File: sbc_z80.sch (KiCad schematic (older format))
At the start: 61 parts, among them J1 RC80 Bus, J3 PIO Header, J4 Conn_01x06, J5 Conn_01x06, J6 CTC Header, J7 AVR-JTAG-10, SW1 SW_Push, SW2 Config, U1 CPU -Z84C0020AEG, U10 74HC04, U12 MIC811LUY, U3 SRAM - IS62C5128BL-45TLI, U4 SST39SF040, U6 SIO/3 - Z84C4310AEG, U7 CPLD - EPM7032STC44, U8 CTC - Z84C3010AEG, U9 Z84C2010AEG

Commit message: fixed pins
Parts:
- removed J7: AVR-JTAG-10, Connector_PinHeader_1.27mm:PinHeader_2x05_P1.27mm_Vertical, symbol sbc_z80-rescue:AVR-JTAG-10-Connector
- removed R21: 1K, Resistor_SMD:R_0603_1608Metric_Pad1.05x0.95mm_HandSolder, symbol sbc_z80-rescue:R_Small-Device
- removed R22, R23, R24: 10K, Resistor_SMD:R_0603_1608Metric_Pad1.05x0.95mm_HandSolder, symbol sbc_z80-rescue:R_Small-Device
- added J?: AVR-JTAG-10, Connector_PinHeader_1.27mm:PinHeader_2x05_P1.27mm_Vertical, symbol sbc_z80-rescue:AVR-JTAG-10-Connector
- added R?: 1K, Resistor_SMD:R_0603_1608Metric_Pad1.05x0.95mm_HandSolder, symbol sbc_z80-rescue:R_Small-Device
- added R? (x3): 10K, Resistor_SMD:R_0603_1608Metric_Pad1.05x0.95mm_HandSolder, symbol sbc_z80-rescue:R_Small-Device
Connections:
- wire segments 513 -> 490
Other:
- moved on the sheet: R31, R32, R33, R34, R35, R36, R5, R6, R7, R8, SW2, U1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

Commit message: changed part layout, removed switch
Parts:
- removed C10: 100nF, Capacitor_SMD:C_0603_1608Metric_Pad1.05x0.95mm_HandSolder, symbol sbc_z80-rescue:C_Small-Device
- removed J5: Conn_01x06, Connector_PinHeader_2.54mm:PinHeader_1x06_P2.54mm_Horizontal, symbol sbc_z80-rescue:Conn_01x06-Connector_Generic
- removed J?: AVR-JTAG-10, Connector_PinHeader_1.27mm:PinHeader_2x05_P1.27mm_Vertical, symbol sbc_z80-rescue:AVR-JTAG-10-Connector
- removed R10, R11, R12, R13, R17, R19: 2K2, Resistor_SMD:R_0603_1608Metric_Pad1.05x0.95mm_HandSolder, symbol sbc_z80-rescue:R_Small-Device
- removed R15, R20: 100K, Resistor_SMD:R_0603_1608Metric_Pad1.05x0.95mm_HandSolder, symbol sbc_z80-rescue:R_Small-Device
- removed R?: 1K, Resistor_SMD:R_0603_1608Metric_Pad1.05x0.95mm_HandSolder, symbol sbc_z80-rescue:R_Small-Device
- removed R? (x3): 10K, Resistor_SMD:R_0603_1608Metric_Pad1.05x0.95mm_HandSolder, symbol sbc_z80-rescue:R_Small-Device
- removed SW1: SW_Push, Button_Switch_SMD:SW_SPST_FSMSM, symbol sbc_z80-rescue:SW_Push-Switch
- removed SW2: Config, Button_Switch_SMD:SW_DIP_SPSTx06_Slide_Copal_CHS-06A_W5.08mm_P1.27mm_JPin, symbol sbc_z80-rescue:SW_DIP_x06-Switch
- removed U12: MIC811LUY, Package_TO_SOT_SMD:SOT-143, symbol sbc_z80-rescue:MIC811LUY-Power_Supervisor
- added C6: 100nF, Capacitor_SMD:C_0603_1608Metric_Pad1.05x0.95mm_HandSolder, symbol sbc_z80-rescue:C_Small-Device
- added C7: 2.2uF, Capacitor_SMD:C_0603_1608Metric_Pad1.05x0.95mm_HandSolder, symbol max_breakout-rescue:C_Small-Device
- added D1, D10, D11, D4, D5, D6, D7, D8, D9: Green, LED_SMD:LED_0603_1608Metric_Pad1.05x0.95mm_HandSolder, symbol max_breakout-rescue:LED-Device
- added D2: LED, LED_SMD:LED_0603_1608Metric_Pad1.05x0.95mm_HandSolder, symbol Device:LED
- added J3: AVR-JTAG-10, Connector_PinHeader_2.54mm:PinHeader_2x05_P2.54mm_Vertical, symbol max_breakout-rescue:AVR-JTAG-10-Connector
- added J4: IDE, Connector_PinHeader_2.54mm:PinHeader_2x20_P2.54mm_Horizontal, symbol Connector_Generic:Conn_02x20_Odd_Even
- added J7: Conn_01x06, Connector_PinHeader_2.54mm:PinHeader_1x06_P2.54mm_Horizontal, symbol sbc_z80-rescue:Conn_01x06-Connector_Generic
- added JP1: Jumper_NC_Small, Connector_PinHeader_1.27mm:PinHeader_1x02_P1.27mm_Vertical, symbol Device:Jumper_NC_Small
- added Q1: IRLML6402, Package_TO_SOT_SMD:SOT-23, symbol max_breakout-rescue:IRLML6402-Transistor_FET
- added R10: 1K, Resistor_SMD:R_0603_1608Metric_Pad1.05x0.95mm_HandSolder, symbol max_breakout-rescue:R_Small-Device
- added R12, R14, R15: 10K, Resistor_SMD:R_0603_1608Metric_Pad1.05x0.95mm_HandSolder, symbol max_breakout-rescue:R_Small-Device
- added R13, R3: 100R, Resistor_SMD:R_0603_1608Metric_Pad1.05x0.95mm_HandSolder, symbol max_breakout-rescue:R_Small-Device
- added R17: 360R, Resistor_SMD:R_0603_1608Metric_Pad1.05x0.95mm_HandSolder, symbol max_breakout-rescue:R_Small-Device
- added R21, R22, R6, R8, R9: 10K, Resistor_SMD:R_0603_1608Metric_Pad1.05x0.95mm_HandSolder, symbol sbc_z80-rescue:R_Small-Device
- added R23, R24, R25, R29, R30: 680R, Resistor_SMD:R_0603_1608Metric_Pad1.05x0.95mm_HandSolder, symbol sbc_z80-rescue:R_Small-Device
- added R37, R38: 2K2, Resistor_SMD:R_0603_1608Metric_Pad1.05x0.95mm_HandSolder, symbol sbc_z80-rescue:R_Small-Device
- added R40, R42: 100K, Resistor_SMD:R_0603_1608Metric_Pad1.05x0.95mm_HandSolder, symbol sbc_z80-rescue:R_Small-Device
- added SW1: Reset, Button_Switch_SMD:SW_Push_SPST_NO_Alps_SKRK, symbol Switch:SW_Push
- added U1: DS1813R-5+T&R, Package_TO_SOT_SMD:SOT-23, symbol max_breakout-rescue:DS1813R-5+T&R-Power_Supervisor
- added U11: 74HCT273, Package_SO:TSSOP-20_4.4x6.5mm_P0.65mm, symbol 74xx:74HCT273
- added U2: AP7381-33SA, Package_TO_SOT_SMD:SOT-23, symbol Regulator_Linear:AP7381-33SA
- added X1: CTX-636 50mhz, Oscillator:Oscillator_SMD_TXC_7C-4Pin_5.0x3.2mm_HandSoldering, symbol Oscillator:TXC-7C
- R16: value 2K2 -> 1K
- R18: value 2K2 -> 10K
- R26, R27, R28: value 10K -> 680R; Description (none) -> Thick Film Resistors - SMD 1K OHM 5%; MFR (none) -> Yageo; MPN (none) -> RC0603JR-071KL; SPN (none) -> 603-RC0603JR-071KL; SPR (none) -> Mouser; SPURL (none) -> https://www.mouser.com/ProductDetail/603-RC0603JR-071KL
- R31, R32, R33, R34, R35, R36: value 10K -> 2K2
- U10: renamed from U9; symbol sbc_z80-rescue:Z84C2010AEG-sbc_z80-rescue -> sbc_z80-rescue:Z84C2010AEG
- U7: renamed from U10; value 74HC04 -> 74HCT2G04; footprint (none) -> Package_SO:TSOP-6_1.65x3.05mm_P0.95mm; symbol sbc_z80-rescue:74HC04-74xx -> 74xGxx:74HCT2G04
- U8: renamed from U4; footprint (none) -> Package_LCC:PLCC-32_SMD-Socket
- renumbered C5 to C1, C13 to C10, C14 to C11, C6 to C2, C7 to C3, C8 to C4, C9 to C5, C11 to C8, C12 to C9, D1 to D3, J6 to J2, J3 to J5, J4 to J6, R5 to R1, R4 to R11, R29 to R19, R8 to R2, R30 to R20, R9 to R39, R7 to R4, R14 to R41, R6 to R5, R25 to R7, U1 to U3, U8 to U4, U7 to U5, U3 to U6, U6 to U9
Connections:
- net labels added: 3V3, CLK_50, CLK_CPU, DO, D_LED, ~ACTIVE, ~CF, ~PIO_RST
- net labels removed: +5V, CLK_F, SW0, SW1, SW2, SW3, SW4, SW5, SW6, ~DIO
- wire segments 490 -> 568
- no-connect marks 18 -> 25
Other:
- note added: "50Mhz Clock"
- note added: "IDE/CF"
- note added: "JTAG"
- note added: "JTAG Activity"
- moved on the sheet: C1, C10, C11, C2, C3, C4, C5, C8, C9, D3, J1, J2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

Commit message: added USB power, fixed layout
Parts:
- added C12: 100nF, Capacitor_SMD:C_0603_1608Metric_Pad1.05x0.95mm_HandSolder, symbol Device:C_Small
- added C13: 10uF, Capacitor_SMD:C_0603_1608Metric_Pad1.05x0.95mm_HandSolder, symbol Device:C_Small
- added C14: 1uF, Capacitor_SMD:C_0603_1608Metric_Pad1.05x0.95mm_HandSolder, symbol Device:C_Small
- added J8: USB_B_Micro, Connector_USB:USB_Micro-B_Molex-105017-0001, symbol Connector:USB_B_Micro
- added R43: 1M, Resistor_SMD:R_0603_1608Metric_Pad1.05x0.95mm_HandSolder, symbol sbc_z80-rescue:R_Small-Device
- added U12: MAX40200AUK, Package_TO_SOT_SMD:SOT-23-5_HandSoldering, symbol Analog_Switch:MAX40200AUK
- C7: symbol max_breakout-rescue:C_Small-Device -> sbc_z80-rescue:C_Small-Device-max_breakout-rescue
- D1, D10, D11, D4, D5, D6, D7, D8, D9: symbol max_breakout-rescue:LED-Device -> sbc_z80-rescue:LED-Device-max_breakout-rescue
- J3: symbol max_breakout-rescue:AVR-JTAG-10-Connector -> sbc_z80-rescue:AVR-JTAG-10-Connector-max_breakout-rescue
- Q1: symbol max_breakout-rescue:IRLML6402-Transistor_FET -> sbc_z80-rescue:IRLML6402-Transistor_FET-max_breakout-rescue
- R10, R12, R13, R14, R15, R17, R3: symbol max_breakout-rescue:R_Small-Device -> sbc_z80-rescue:R_Small-Device-max_breakout-rescue
- U1: symbol max_breakout-rescue:DS1813R-5+T&R-Power_Supervisor -> sbc_z80-rescue:DS1813R-5+T&R-Power_Supervisor-max_breakout-rescue
- U2: symbol Regulator_Linear:AP7381-33SA -> sbc_z80-rescue:AP7381-33SA-Regulator_Linear
- U7: symbol 74xGxx:74HCT2G04 -> sbc_z80-rescue:74HCT2G04-74xGxx
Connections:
- net labels added: +5V
- wire segments 568 -> 588
- no-connect marks 25 -> 28
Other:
- note added: "Power"
- moved on the sheet: C1, C10, C11, C2, C3, C4, C5, C6, C7, C8, C9, D2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

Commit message: routing
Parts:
- added C15, C16: 100nF, Capacitor_SMD:C_0603_1608Metric_Pad1.05x0.95mm_HandSolder, symbol sbc_z80-rescue:C_Small-Device
- J6: value Conn_01x06 -> Port A
- J7: value Conn_01x06 -> Port B
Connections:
- wire segments 588 -> 592
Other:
- moved on the sheet: C1, C10, C11, C2, C3, C4, C5, C6, C8, C9, D10, D11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

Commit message: more routing
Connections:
- net labels removed: CLK
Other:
- moved on the sheet: J1

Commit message: routed...
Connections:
- net labels removed: +5V
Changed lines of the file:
@@
 CLK_CPU
 Text Label 3500 9625 0    50   ~ 0
-~SIO
+~CTC
 Text Label 3500 10425 0    50   ~ 0
 IEO
@@
 	2500 3300 2500 3350
 Connection ~ 2500 3300
-$Comp
-L power:+5V #PWR0116
-U 1 1 5CB7C89C
-P 2500 2600
-AR Path="/5CB7C89C" Ref="#PWR0116"  Part="1"
-AR Path="/5CB63856/5CB7C89C" Ref="#PWR?"  Part="1"
-AR Path="/5CB5AB00/5CB63856/5CB7C89C" Ref="#PWR?"  Part="1"
-F 0 "#PWR0116" H 2500 2450 50  0001 C CNN
-F 1 "+5V" H 2515 2773 50  0000 C CNN
-F 2 "" H 2500 2600 50  0001 C CNN
-F 3 "" H 2500 2600 50  0001 C CNN
-	1    2500 2600
-	1    0    0    -1
-$EndComp
 Wire Wire Line
 	1400 2900 1400 3100
@@
 Wire Notes Line
 	600  4050 2850 4050
-Connection ~ 2500 2600
 $Comp
 L power:PWR_FLAG #FLG0101
@@
 Wire Wire Line
 	2600 10800 2800 10800
+$Comp
+L power:VCC #PWR0101
+U 1 1 5D50F790
+P 2500 2600
+F 0 "#PWR0101" H 2500 2450 50  0001 C CNN
+F 1 "VCC" H 2500 2750 50  0000 C CNN
+F 2 "" H 2500 2600 50  0001 C CNN
+F 3 "" H 2500 2600 50  0001 C CNN
+	1    2500 2600
+	1    0    0    -1
+$EndComp
+Connection ~ 2500 2600
 $EndSCHEMATC

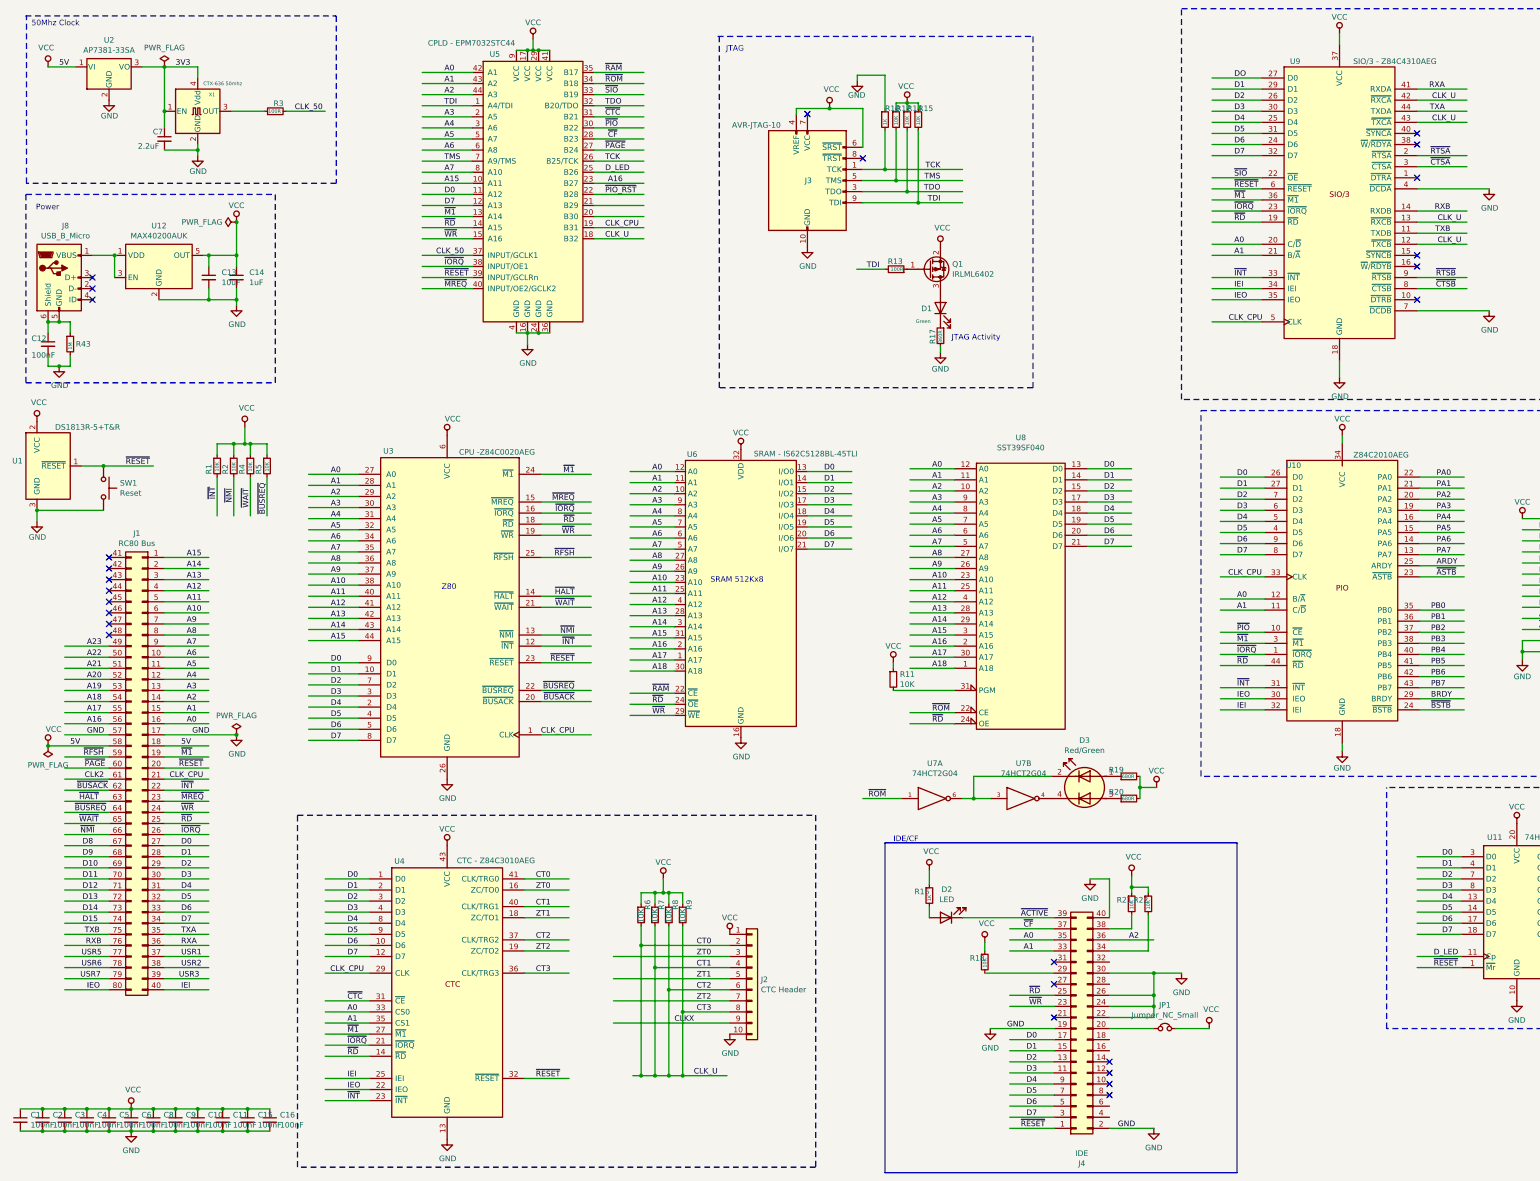
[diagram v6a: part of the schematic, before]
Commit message: passed drc
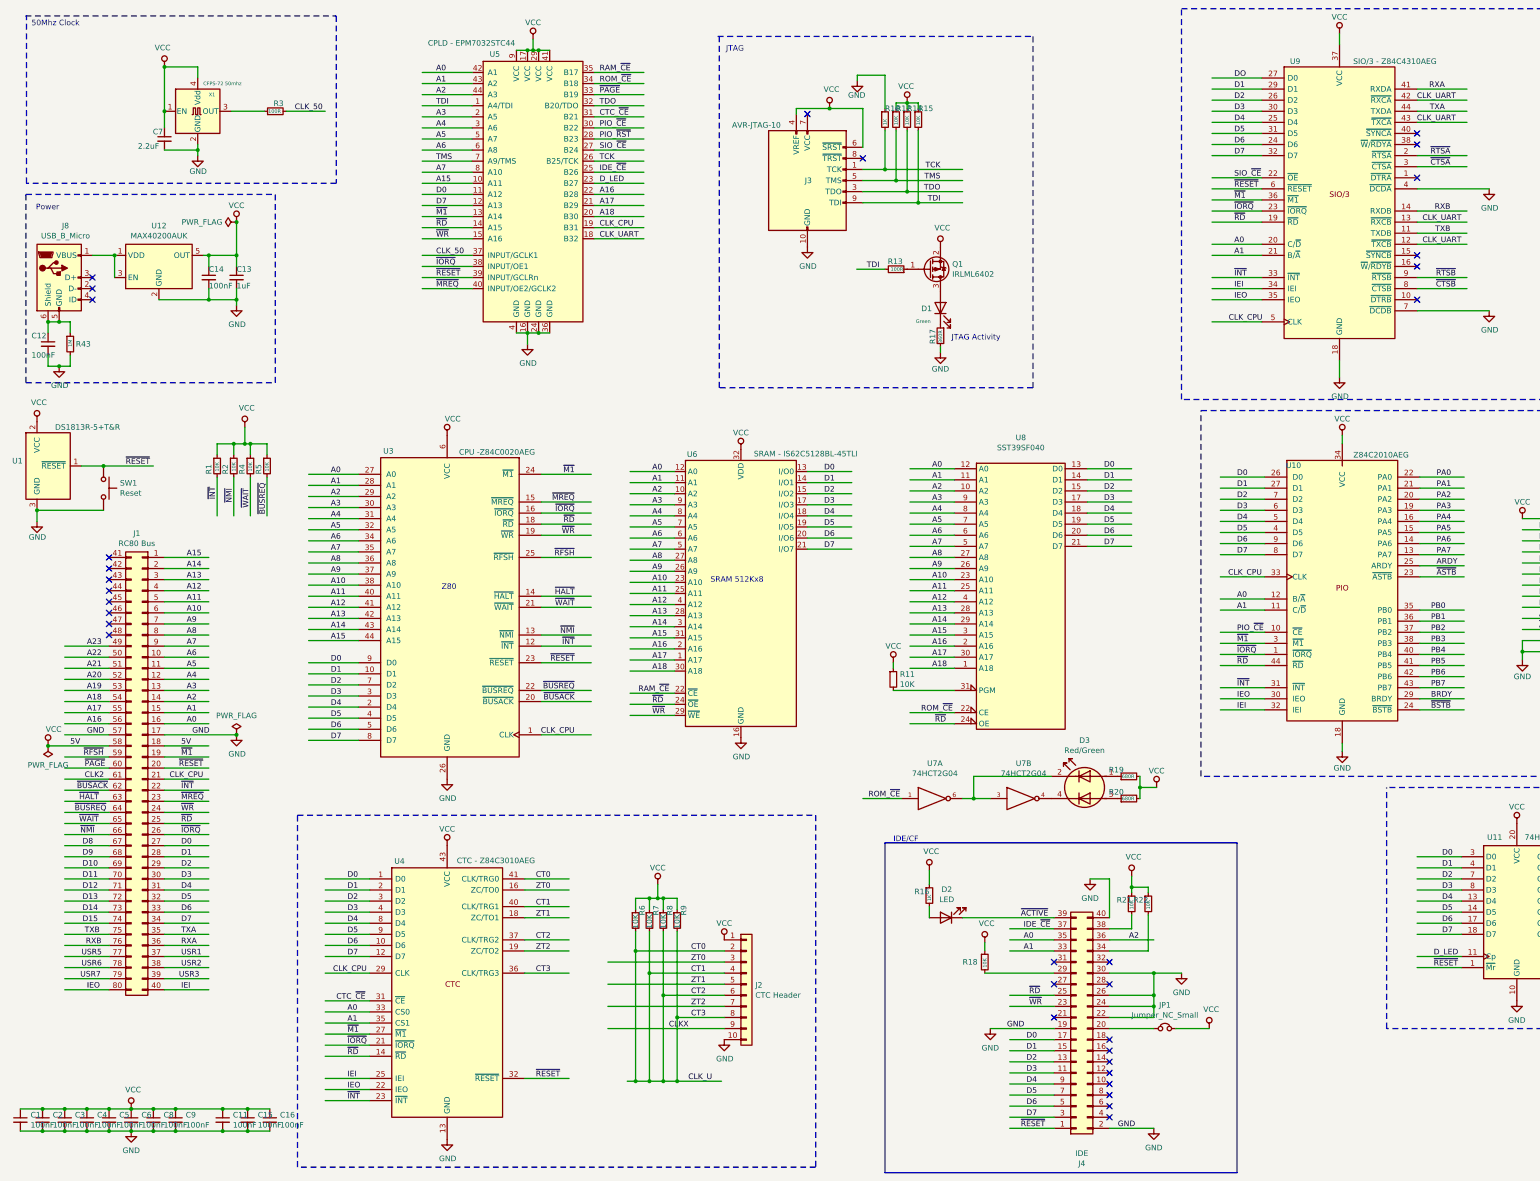
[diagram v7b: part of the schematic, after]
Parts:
- removed C10: 100nF, Capacitor_SMD:C_0603_1608Metric_Pad1.05x0.95mm_HandSolder, symbol sbc_z80-rescue:C_Small-Device
- removed U2: AP7381-33SA, Package_TO_SOT_SMD:SOT-23, symbol sbc_z80-rescue:AP7381-33SA-Regulator_Linear
- C13: value 10uF -> 1uF
- C14: value 1uF -> 100nF
- JP1: footprint Connector_PinHeader_1.27mm:PinHeader_1x02_P1.27mm_Vertical -> Connector_PinHeader_2.54mm:PinHeader_1x02_P2.54mm_Vertical
- X1: value CTX-636 50mhz -> CFPS-72 50mhz; footprint Oscillator:Oscillator_SMD_TXC_7C-4Pin_5.0x3.2mm_HandSoldering -> Oscillator:Oscillator_SMD_SeikoEpson_SG8002CA-4Pin_7.0x5.0mm_HandSoldering
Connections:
- net labels added: CLK_UART, CTC_~CE~, IDE_~CE~, PIO_~CE~, PIO_~RST~, RAM_~CE~, ROM_~CE~, SIO_~CE~
- net labels removed: 3V3, ~CF, ~CTC, ~PIO, ~PIO_RST, ~RAM, ~ROM, ~SIO
- wire segments 592 -> 588
- no-connect marks 28 -> 34
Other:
- moved on the sheet: C13, C14, J2, R6, R7, R8, R9

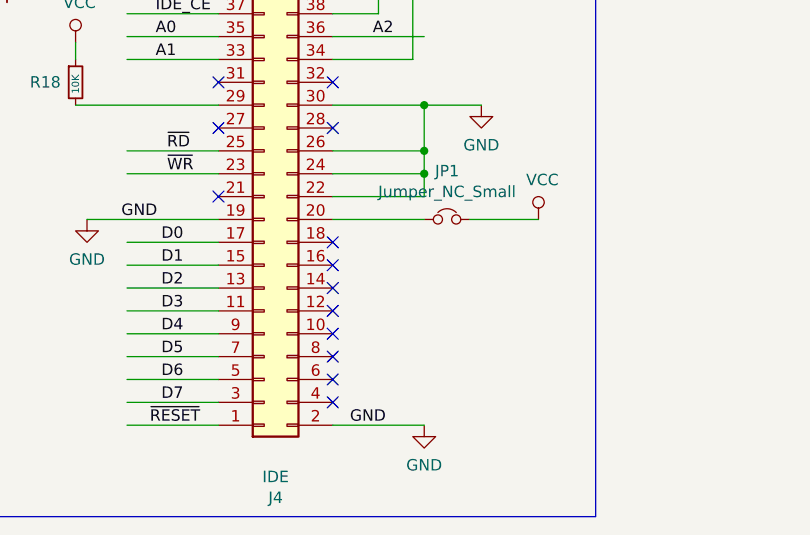
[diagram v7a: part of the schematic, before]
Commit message: fixed layout, added labels
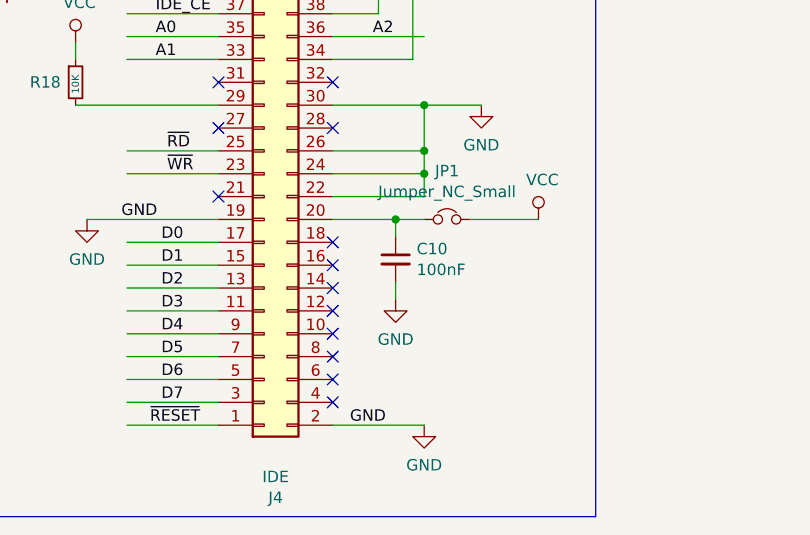
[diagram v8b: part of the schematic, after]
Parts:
- added C10: 100nF, Capacitor_SMD:C_0603_1608Metric_Pad1.05x0.95mm_HandSolder, symbol sbc_z80-rescue:C_Small-Device
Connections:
- wire segments 588 -> 591
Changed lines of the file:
@@
 Sheet 1 1
 Title "THS-80"
-Date "2019-05-06"
-Rev ""
+Date "2019-08-13"
+Rev "1.0"
 Comp "Hyiger Designs"
 Comment1 ""
@@
 	10775 9675 10375 9675
 Wire Wire Line
-	10775 9875 10375 9875
+	10775 9875 10650 9875
 Wire Wire Line
 	10775 9775 10375 9775
@@
 NoConn ~ 10375 10675
 NoConn ~ 10375 10575
+$Comp
+L sbc_z80-rescue:C_Small-Device C?
+U 1 1 5D65939B
+P 10650 10050
+AR Path="/5D65A6A0/5D65939B" Ref="C?"  Part="1"
+AR Path="/5D65939B" Ref="C10"  Part="1"
+F 0 "C10" H 10742 10096 50  0000 L CNN
+F 1 "100nF" H 10742 10005 50  0000 L CNN
+F 2 "Capacitor_SMD:C_0603_1608Metric_Pad1.05x0.95mm_HandSolder" H 10650 10050 50  0001 C CNN
+F 3 "https://www.mouser.com/datasheet/2/396/mlcc02_e-1307760.pdf" H 10650 10050 50  0001 C CNN
+F 4 "Multilayer Ceramic Capacitors MLCC - SMD/SMT 0603 6.3V 0.47uF 10% X7R" H 10742 10196 50  0001 C CNN "Description"
+F 5 "Taiyo Yuden" H 10650 10050 50  0001 C CNN "MFR"
+F 6 "JMK107B7474KA-T" H 10650 10050 50  0001 C CNN "MPN"
+F 7 "963-JMK107B7474KA-T" H 10742 10196 50  0001 C CNN "SPN"
+F 8 "Mouser" H 10650 10050 50  0001 C CNN "SPR"
+F 9 "https://www.mouser.com/ProductDetail/963-JMK107B7474KA-T" H 10742 10196 50  0001 C CNN "SPURL"
+	1    10650 10050
+	1    0    0    -1
+$EndComp
+Wire Wire Line
+	10650 9950 10650 9875
+Connection ~ 10650 9875
+Wire Wire Line
+	10650 9875 10375 9875
+$Comp
+L sbc_z80-rescue:GND-power #PWR05
+U 1 1 5D65A340
+P 10650 10225
+AR Path="/5D65A340" Ref="#PWR05"  Part="1"
+AR Path="/5CB63856/5D65A340" Ref="#PWR?"  Part="1"
+AR Path="/5CB5AB00/5CB63856/5D65A340" Ref="#PWR?"  Part="1"
+AR Path="/5CFABACD/5D65A340" Ref="#PWR?"  Part="1"
+AR Path="/5CF9C1ED/5D65A340" Ref="#PWR?"  Part="1"
+F 0 "#PWR05" H 10650 9975 50  0001 C CNN
+F 1 "GND" H 10650 10050 50  0000 C CNN
+F 2 "" H 10650 10225 50  0001 C CNN
+F 3 "" H 10650 10225 50  0001 C CNN
+	1    10650 10225
+	1    0    0    -1
+$EndComp
+Wire Wire Line
+	10650 10150 10650 10225
 $EndSCHEMATC
